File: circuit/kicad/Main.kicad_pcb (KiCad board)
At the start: 2 copper layers, 110.8 x 117 mm, 104 parts, among them J1 SH3, J10 PA3, J11 SH4, J2 SH3, J3 FFC6, J4 SH6, J5 FTSH2x5, J6 FFC4, J7 SH4, J8 FFC12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

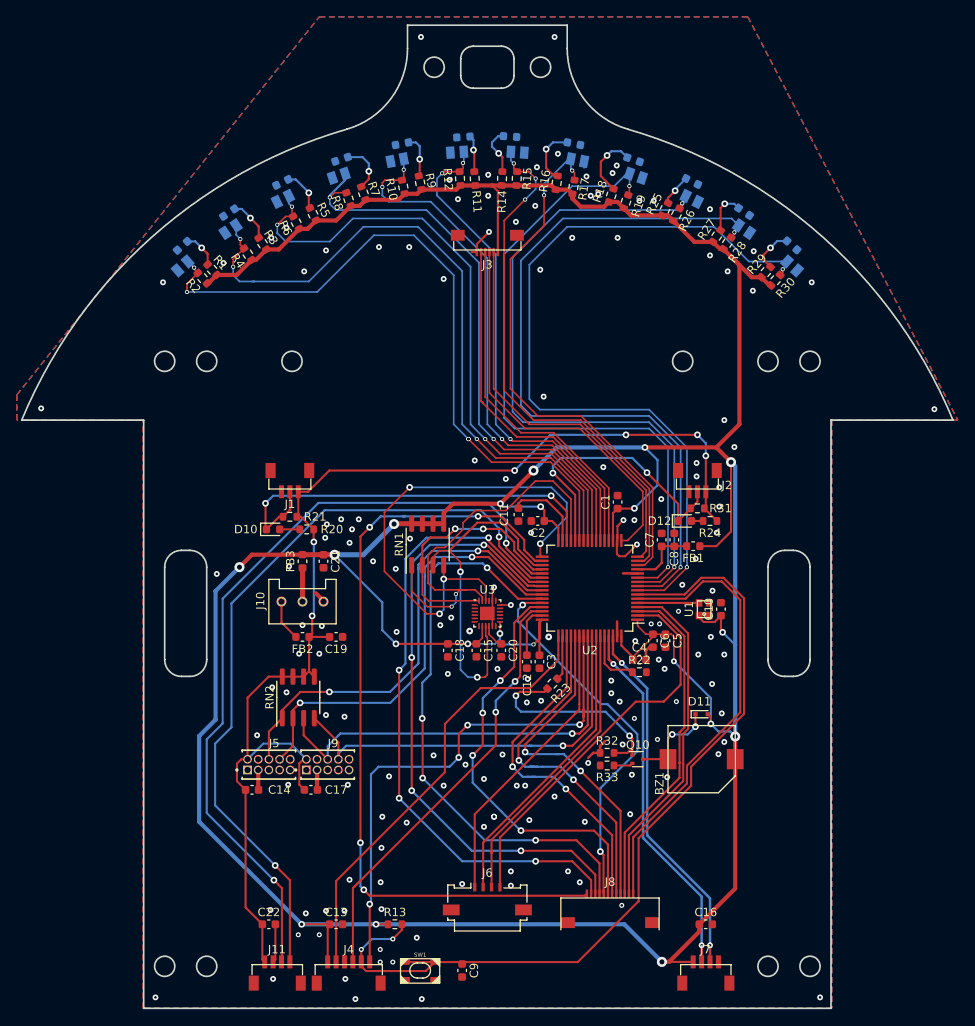
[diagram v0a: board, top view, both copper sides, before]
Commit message: フットプリントの問題は解消
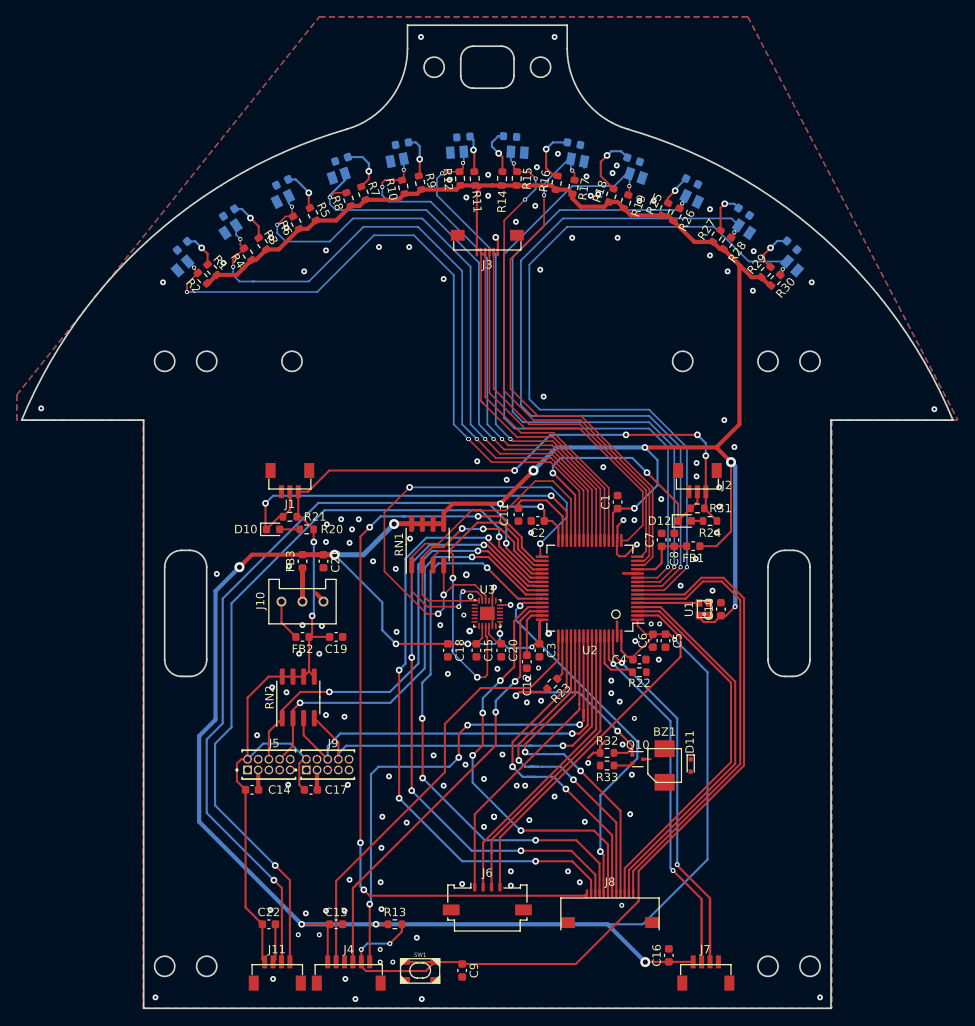
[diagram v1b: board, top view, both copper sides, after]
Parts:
- moved D11 6.24 mm to (24.2, 18.1), turned to 270 degrees
- moved C16 5.75 mm to (21.6, 40.7), turned to 90 degrees
- moved BZ1 4.46 mm to (21.1, 18.1), turned to 270 degrees
- moved C3 1.35 mm to (6.20, 4.40)
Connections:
- J3 pad 1: +3V3 -> GND
- J3 pad 6: GND -> +3V3
- J5 pad 1: (no net) -> Net-(J5-Pad1)
- J5 pad 10: (no net) -> Net-(J5-Pad10)
- J5 pad 4: (no net) -> Net-(J5-Pad4)
- J5 pad 5: (no net) -> Net-(J5-Pad5)
- J5 pad 7: (no net) -> Net-(J5-Pad7)
- J5 pad 9: (no net) -> Net-(J5-Pad9)
- J9 pad 1: (no net) -> Net-(J9-Pad1)
- J9 pad 10: (no net) -> Net-(J9-Pad10)
- J9 pad 4: (no net) -> Net-(J9-Pad4)
- J9 pad 5: (no net) -> Net-(J9-Pad5)
- J9 pad 7: (no net) -> Net-(J9-Pad7)
- J9 pad 9: (no net) -> Net-(J9-Pad9)
- U1 pad 1: (no net) -> Net-(U1-Pad1)
- U3 pad 1: (no net) -> Net-(U3-Pad1)
- U3 pad 12: (no net) -> Net-(U3-Pad12)
- U3 pad 14: (no net) -> Net-(U3-Pad14)
- U3 pad 15: (no net) -> Net-(U3-Pad15)
- U3 pad 16: (no net) -> Net-(U3-Pad16)
- U3 pad 17: (no net) -> Net-(U3-Pad17)
- U3 pad 19: (no net) -> Net-(U3-Pad19)
- U3 pad 2: (no net) -> Net-(U3-Pad2)
- U3 pad 21: (no net) -> Net-(U3-Pad21)
- U3 pad 3: (no net) -> Net-(U3-Pad3)
- U3 pad 4: (no net) -> Net-(U3-Pad4)
- U3 pad 5: (no net) -> Net-(U3-Pad5)
- U3 pad 6: (no net) -> Net-(U3-Pad6)
- U3 pad 7: (no net) -> Net-(U3-Pad7)
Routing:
- net +3V3: track 465.7 -> 442.9 mm, vias 20 -> 18
- net Net-(BZ1-Pad2): track 10.7 -> 0.90 mm, vias 2 -> 0
- net ICM_SCLK: track 49.6 -> 44.2 mm
- net /SW1: track 40.4 -> 45.0 mm
- net /SW2: track 41.2 -> 45.8 mm
- net GND: track 37.5 -> 34.3 mm, vias 157 -> 147
- net /DRV2_EN: track 46.8 -> 44.8 mm
- net Net-(Q10-Pad1): track 25.2 -> 24.3 mm
- net ICM_MOSI: track 30.6 -> 29.8 mm
- net ICM_MISO: track 42.7 -> 42.1 mm
- net ICM_nCS: track 60.3 -> 59.7 mm

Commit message: 後はガーバデータ出してロゴ刺すだけ
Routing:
- net +3V3: track 442.9 -> 452.3 mm, vias 18 -> 19
- net Net-(BZ1-Pad2): track 0.90 -> 6.70 mm
- net GND: vias 147 -> 163

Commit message: export
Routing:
- net /Sensor01: track 83.1 -> 84.2 mm, vias 4 -> 3
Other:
- rule via_min_size: 0.1524 -> 0.6

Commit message: hoge
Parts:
- moved J10 3.90 mm to (-25.9, -1.40)
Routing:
- net Net-(FB2-Pad1): track 5.01 -> 8.47 mm
- net Net-(FB3-Pad1): track 3.91 -> 5.63 mm
- net GND: track 34.3 -> 33.0 mm, vias 163 -> 166
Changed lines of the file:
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@@
     (thickness 1.6)
     (drawings 75)
-    (tracks 1289)
+    (tracks 1293)
     (zones 0)
     (modules 104)
@@
       (drillshape 0)
       (scaleselection 1)
-      (outputdirectory "Gerber/"))
+      (outputdirectory "Gerber/Main/"))
   )
   (net 0 "")
@@
   )
   (module PA:PA_01x03 (layer F.Cu)
-    (at -22 -1.4 180)
+    (at -25.9 -1.4 180)
     (fp_text reference J10 (at 5 0.1 90) (layer F.SilkS)
       (effects (font (size 1 1) (thickness 0.15)))
@@
   (via (at -17.4 -11.2) (size 0.7) (drill 0.3) (layers F.Cu B.Cu) (net 3))
   (via (at -19.2 -8.5) (size 0.7) (drill 0.3) (layers F.Cu B.Cu) (net 3))
-  (via (at -22 1.4) (size 0.7) (drill 0.3) (layers F.Cu B.Cu) (net 3))
   (via (at -13.6 -6.2) (size 0.7) (drill 0.3) (layers F.Cu B.Cu) (net 3))
   (via (at -9.2 -8.9) (size 0.7) (drill 0.3) (layers F.Cu B.Cu) (net 3))
@@
   (via (at -22.4 4.8) (size 0.7) (drill 0.3) (layers F.Cu B.Cu) (net 3))
   (via (at -20 4.8) (size 0.7) (drill 0.3) (layers F.Cu B.Cu) (net 3))
-  (via (at -19.7 1.5) (size 0.7) (drill 0.3) (layers F.Cu B.Cu) (net 3))
-  (segment (start -19.5 -1.5) (end -20.4 -2.4) (width 0.5) (layer F.Cu) (net 3) (status 10))
   (via (at -1.2 -18.1) (size 0.7) (drill 0.3) (layers F.Cu B.Cu) (net 3))
   (via (at 13.8 -17.4) (size 0.7) (drill 0.3) (layers F.Cu B.Cu) (net 3))
@@
   (via (at 19.2 -17.9) (size 0.6) (drill 0.3) (layers F.Cu B.Cu) (net 3))
   (via (at 2.45 -16) (size 0.6) (drill 0.3) (layers F.Cu B.Cu) (net 3))
+  (via (at -19.6 1.4) (size 0.8) (drill 0.4) (layers F.Cu B.Cu) (net 3))
+  (via (at -22.1 1.1) (size 0.8) (drill 0.4) (layers F.Cu B.Cu) (net 3))
+  (via (at -29.3 -0.1) (size 0.8) (drill 0.4) (layers F.Cu B.Cu) (net 3))
+  (via (at -27.5 -2.9) (size 0.8) (drill 0.4) (layers F.Cu B.Cu) (net 3))
+  (via (at -33.6 8) (size 0.8) (drill 0.4) (layers F.Cu B.Cu) (net 3))
   (segment (start 17.875 -5.25) (end 20 -5.25) (width 0.25) (layer F.Cu) (net 4) (status 10))
   (segment (start 20.75 -6) (end 20.75 -7.975) (width 0.25) (layer F.Cu) (net 4) (status 20))
@@
   (segment (start -20.675 -8.525) (end -20.65 -8.5) (width 0.25) (layer F.Cu) (net 8))
   (segment (start -20.675 -10) (end -20.675 -8.525) (width 0.25) (layer F.Cu) (net 8) (status 10))
-  (via (at -20.85 0.3) (size 0.8) (drill 0.4) (layers F.Cu B.Cu) (net 8))
   (segment (start -20.65 0.1) (end -20.85 0.3) (width 0.25) (layer B.Cu) (net 8))
   (segment (start -20.65 -8.5) (end -20.65 0.1) (width 0.25) (layer B.Cu) (net 8))
@@
   (segment (start 24.65 -21.25) (end 25.3 -20.6) (width 0.25) (layer F.Cu) (net 8))
   (segment (start 16.5 -21.25) (end 24.65 -21.25) (width 0.25) (layer F.Cu) (net 8))
+  (via (at -20.85 0.3) (size 0.8) (drill 0.4) (layers F.Cu B.Cu) (net 8))
   (segment (start 1.326557 3.625) (end 1.65 3.625) (width 0.2) (layer F.Cu) (net 9) (status 30))
   (segment (start 0.2 2.498443) (end 1.326557 3.625) (width 0.2) (layer F.Cu) (net 9) (status 20))
@@
   (segment (start 32.85 -42.089294) (end 33.694501 -41.244793) (width 0.25) (layer F.Cu) (net 25) (status 20))
   (segment (start 32.85 -42.65) (end 32.85 -42.089294) (width 0.25) (layer F.Cu) (net 25))
-  (segment (start -24.5 1.0875) (end -22.7875 2.8) (width 0.25) (layer F.Cu) (net 26) (status 20))
-  (segment (start -24.5 -1.5) (end -24.5 1.0875) (width 0.25) (layer F.Cu) (net 26) (status 10))
-  (segment (start -22 -1.5) (end -22 -5.4125) (width 0.6) (layer F.Cu) (net 27) (status 30))
+  (segment (start -26.1 2.8) (end -22.7875 2.8) (width 0.25) (layer F.Cu) (net 26))
+  (segment (start -28.4 0.5) (end -26.1 2.8) (width 0.25) (layer F.Cu) (net 26))
+  (segment (start -28.4 -1.4) (end -28.4 0.5) (width 0.25) (layer F.Cu) (net 26))
+  (segment (start -22 -5.3) (end -22 -5.4125) (width 0.6) (layer F.Cu) (net 27))
+  (segment (start -25.9 -1.4) (end -22 -5.3) (width 0.6) (layer F.Cu) (net 27))
   (segment (start 18.25 -6.75) (end 17.875 -6.75) (width 0.2) (layer F.Cu) (net 28) (status 30))
   (segment (start 18.89001 -7.39001) (end 18.25 -6.75) (width 0.2) (layer F.Cu) (net 28) (status 20))
@@
   (segment (start -24.5 41.475) (end -24.44999 41.42499) (width 0.25) (layer F.Cu) (net 57) (status 30))
   (via (at -25.4 31.75) (size 0.8) (drill 0.4) (layers F.Cu B.Cu) (net 57))
-  (segment (start 2.25 -8.35) (end 2.25 -11) (width 0.25) (layer B.Cu) (net 57))
-  (segment (start 2.25 -11) (end 0.1 -13.15) (width 0.25) (layer B.Cu) (net 57))
   (segment (start -33.4 23.75) (end -25.4 31.75) (width 0.25) (layer B.Cu) (net 57))
-  (segment (start 0.1 -13.15) (end -20.1 -13.15) (width 0.25) (layer B.Cu) (net 57))
-  (segment (start -20.1 -13.15) (end -31.5 -1.75) (width 0.25) (layer B.Cu) (net 57))
-  (segment (start -31.5 -1.75) (end -31.5 13.1) (width 0.25) (layer B.Cu) (net 57))
-  (segment (start -31.5 13.1) (end -33.4 15) (width 0.25) (layer B.Cu) (net 57))
   (segment (start -33.4 15) (end -33.4 23.75) (width 0.25) (layer B.Cu) (net 57))
+  (segment (start -31.5 -1.9) (end -31.5 13.1) (width 0.25) (layer B.Cu) (net 57))
+  (segment (start -20.25 -13.15) (end -31.5 -1.9) (width 0.25) (layer B.Cu) (net 57))
+  (segment (start 0.1 -13.15) (end -20.25 -13.15) (width 0.25) (layer B.Cu) (net 57))
+  (segment (start 2.25 -11) (end 0.1 -13.15) (width 0.25) (layer B.Cu) (net 57))
+  (segment (start -31.5 13.1) (end -33.4 15) (width 0.25) (layer B.Cu) (net 57))
+  (segment (start 2.25 -8.35) (end 2.25 -11) (width 0.25) (layer B.Cu) (net 57))
   (segment (start 1.4 -7.988658) (end 1.4 -9.1) (width 0.25) (layer F.Cu) (net 58))
   (segment (start 5.138658 -4.25) (end 1.4 -7.988658) (width 0.25) (layer F.Cu) (net 58))
@@
   (segment (start -32.4 22.850004) (end -25.250004 30) (width 0.25) (layer B.Cu) (net 58))
   (segment (start -32.4 15.5) (end -32.4 22.850004) (width 0.25) (layer B.Cu) (net 58))
-  (segment (start -30.45 13.55) (end -32.4 15.5) (width 0.25) (layer B.Cu) (net 58))
-  (segment (start -19.374999 -12.275001) (end -30.45 -1.2) (width 0.25) (layer B.Cu) (net 58))
-  (segment (start -30.45 -1.2) (end -30.45 13.55) (width 0.25) (layer B.Cu) (net 58))
-  (segment (start -0.775001 -12.275001) (end -19.374999 -12.275001) (width 0.25) (layer B.Cu) (net 58))
+  (segment (start -30.45 -1.65) (end -30.45 13.55) (width 0.25) (layer B.Cu) (net 58))
+  (segment (start -19.824999 -12.275001) (end -30.45 -1.65) (width 0.25) (layer B.Cu) (net 58))
+  (segment (start -0.775001 -12.275001) (end -19.824999 -12.275001) (width 0.25) (layer B.Cu) (net 58))
   (segment (start 1.4 -10.1) (end -0.775001 -12.275001) (width 0.25) (layer B.Cu) (net 58))
+  (segment (start -30.45 13.55) (end -32.4 15.5) (width 0.25) (layer B.Cu) (net 58))
   (segment (start 1.4 -9.1) (end 1.4 -10.1) (width 0.25) (layer B.Cu) (net 58))
   (via (at -34.9 -41.15) (size 0.6) (drill 0.3) (layers F.Cu B.Cu) (net 59))
@@
     (polygon
       (pts
-        (xy -20.9 -8.7) (xy -20.7 -6.6) (xy -24.7 -6.4) (xy -23 -8.8) (xy -21.6 -10.1)
-      )
-    )
-  )
-  (zone (net 0) (net_name "") (layer F.Cu) (hatch edge 0.508)
-    (connect_pads (clearance 0.508))
-    (min_thickness 0.254)
-    (keepout (tracks allowed) (vias allowed) (copperpour not_allowed))
-    (fill (arc_segments 32) (thermal_gap 0.508) (thermal_bridge_width 0.508))
-    (polygon
-      (pts
-        (xy -19.2 -0.6) (xy -21.4 0.7) (xy -22.4 -1) (xy -21.6 -2) (xy -19.8 -2)
+        (xy -20.9 -8.7) (xy -20.7 -6.6) (xy -24.6 -6.6) (xy -23 -8.8) (xy -21.6 -10.1)
       )
     )
@@
       )
     )
-  )
-  (zone (net 0) (net_name "") (layer B.Cu) (hatch edge 0.508)
-    (connect_pads (clearance 0.508))
-    (min_thickness 0.254)
-    (keepout (tracks allowed) (vias allowed) (copperpour not_allowed))
-    (fill (arc_segments 32) (thermal_gap 0.508) (thermal_bridge_width 0.508))
-    (polygon
-      (pts
-        (xy -20.8 -2.1) (xy -22.8 -2.1) (xy -22.8 -7.1) (xy -20.8 -7.1)
-      )
-    )
